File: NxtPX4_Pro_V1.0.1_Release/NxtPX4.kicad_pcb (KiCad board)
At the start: 4 copper layers, 29 x 27 mm, 165 parts, among them J1 USB_C_Receptacle_USB2.0, J10 ESC, J11 Aux GPIO, J12 AUX GPIO, J13 5V, J14 5V, J15 Aux SPI, J16 Buzz, J17 Aux I2C, J18 Aux PWM, J19 GND, J2 Receiver, J20 Aux GPIO 2, J21 GND, J22 Aux GPIO 1, J24 Micro_SD_Card, J3 5V, J4 Cam_Info, J5 9V, J6 Aux UART, J7 Aux UART, J8 Aux UART, J9 Upper computer connector, Q1 AP40P05, Q2 SS8050(NPN BEC), Q3 SS8050(NPN BEC), U1 MP9943GQ-Z, U10 BMI088, U11 ICM-20602, U12 MPU6500, U13 BMP388, U14 W25Q128JVS, U15 Signature, U16 High_temp, U17 high_voltage, U18 Caution, U19 Caution, U2 RT9013-33GB, U3 RT9013-33GB, U4 MP9943GQ-Z, U5 HKU_Logo, U6 UAV_LOGO, U7 Direction_Logo, U8 RI_LOGO, U9 STM32H743VIH6, Y1 SG-210STF/ X1G004171002700, Y2 ABS07 (32.768kHZ)

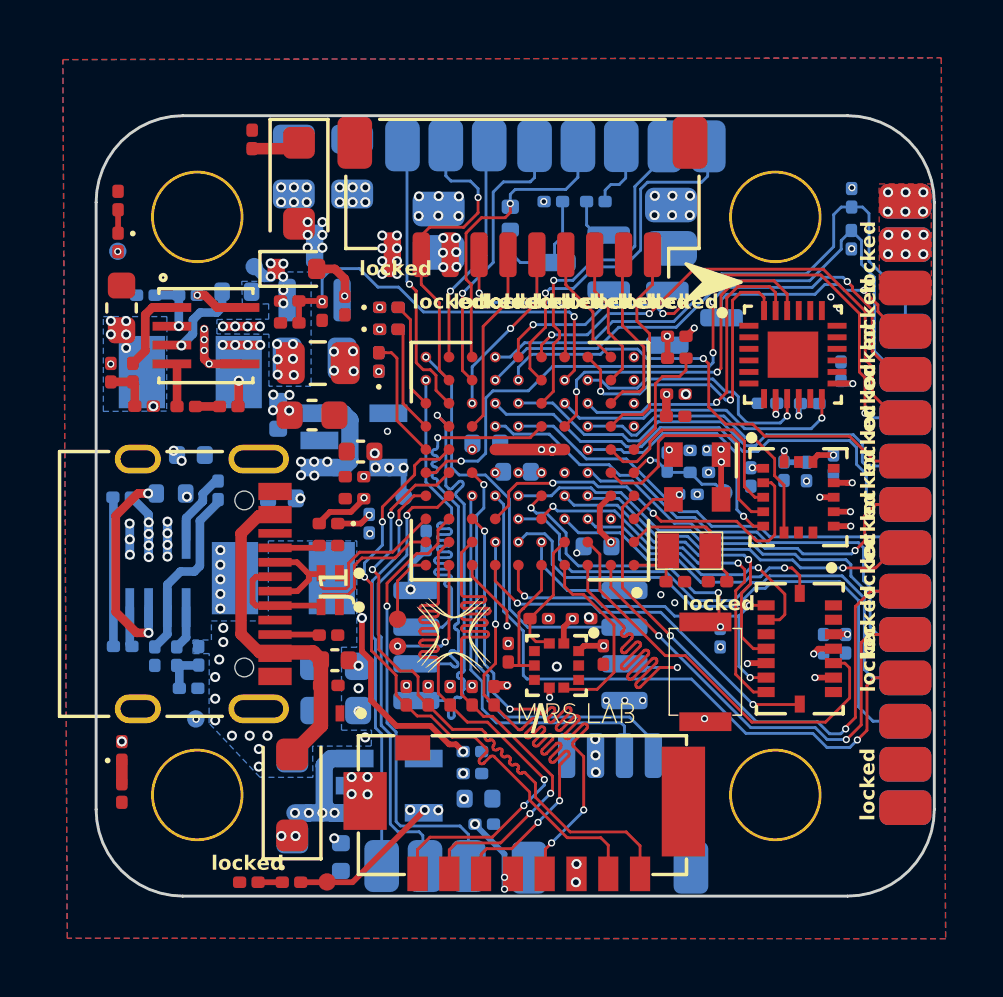
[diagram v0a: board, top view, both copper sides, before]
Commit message: [Fix][other]:Upgrade for JLC manufacturer
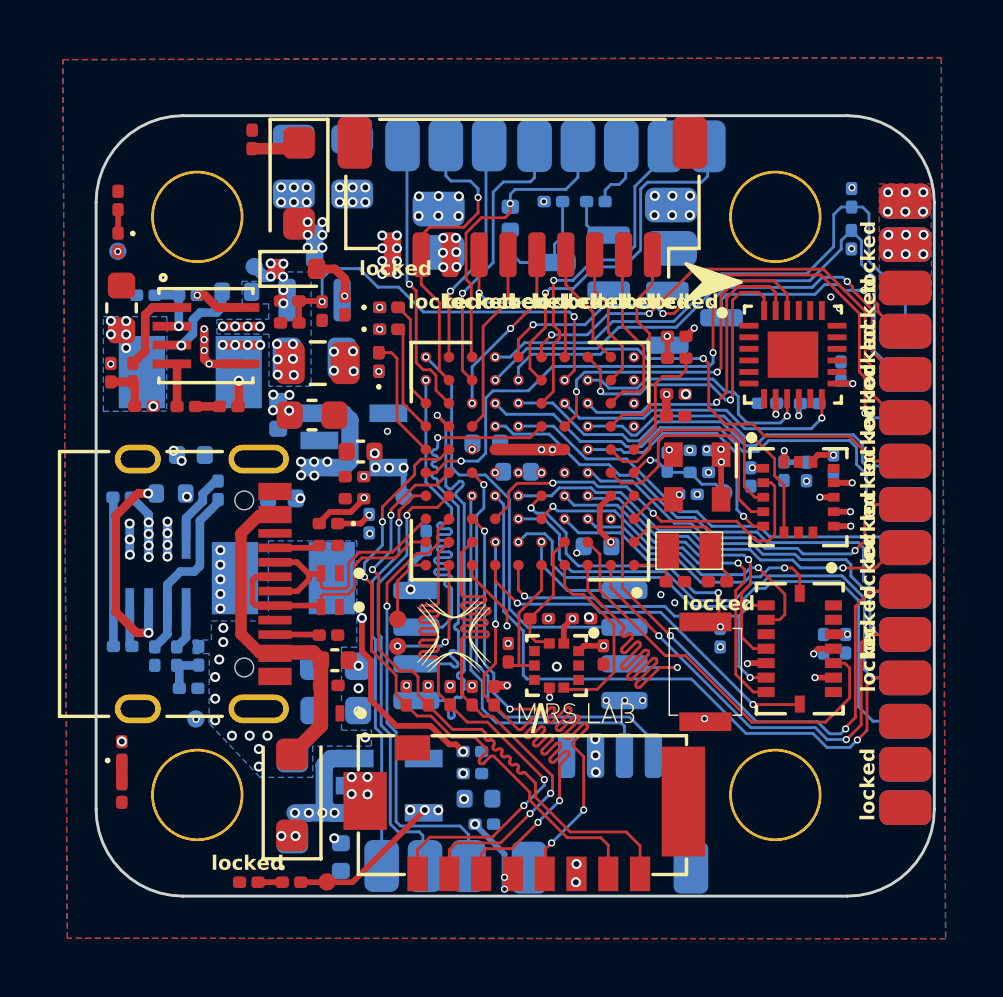
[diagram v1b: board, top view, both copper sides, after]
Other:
- board text removed: "V1.0Release"
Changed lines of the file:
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@@
   (paper "A5")
   (title_block
-    (title "NxtPX4Pro 219 V1.0")
-    (date "2023-02-19")
-    (rev "Peize")
+    (title "NxtPX4Pro 0303 V1.0.1")
+    (date "2023-03-03")
+    (rev "Khalil")
     (company "HKUST DJI")
-    (comment 1 "改善供电结构")
-    (comment 2 "增强供电能力")
-    (comment 3 "发板")
+    (comment 1 "定板")
   )
   (layers
@@
     (property "ki_keywords" "usb universal serial bus type-C USB2.0")
     (attr smd)
-    (fp_text reference "J1" (at 0 -5.715 -90) (layer "F.SilkS")
+    (fp_text reference "J1" (at 0 -5.715 -90) (layer "F.SilkS") hide
         (effects (font (size 1 1) (thickness 0.15)))
     )
@@
     )
   )
-  (footprint "NxtPX4:my_signature" (layer "B.Cu")
+  (footprint "NxtPX4:my_signature" locked (layer "B.Cu")
     (at 113.97 67.93 90)
     (property "Sheetfile" "NxtPX4.kicad_sch")
@@
     (effects (font (size 0.5 0.5) (thickness 0.1) bold) (justify left bottom mirror))
   )
-  (gr_text "V1.0Release" (at 110.25 78.78 270) (layer "B.SilkS")
+  (gr_text locked "V1.0.1\nRelease" (at 109.56 78.82 270) (layer "B.SilkS")
     (effects (font (size 0.5 0.5) (thickness 0.1) bold) (justify left bottom mirror))
   )
@@
     (effects (font (size 0.5 0.5) (thickness 0.1) bold) (justify left bottom mirror))
   )
-  (gr_text locked "GND" (at 99.9 65.11 270) (layer "B.SilkS")
+  (gr_text locked "GND" (at 99.96 65.49 270) (layer "B.SilkS")
     (effects (font (size 0.5 0.5) (thickness 0.1) bold) (justify left bottom mirror))
   )
@@
     (effects (font (size 0.5 0.5) (thickness 0.1) bold) (justify left bottom mirror))
   )
-  (gr_text locked "U5" (at 104.79 62.67 180) (layer "B.SilkS")
+  (gr_text locked "U5" (at 107.95 62.67 180) (layer "B.SilkS")
     (effects (font (size 0.5 0.5) (thickness 0.1) bold) (justify left bottom mirror))
   )
@@
     (effects (font (size 0.5 0.5) (thickness 0.1) bold) (justify left bottom mirror))
   )
-  (gr_text locked "9V" (at 99.98 63.49 270) (layer "B.SilkS")
+  (gr_text locked "9V" (at 99.96 63.67 270) (layer "B.SilkS")
     (effects (font (size 0.5 0.5) (thickness 0.1) bold) (justify left bottom mirror))
   )
@@
     (effects (font (size 0.5 0.5) (thickness 0.1) bold) (justify left bottom))
   )
-  (gr_text locked "I" (at 103.357024 66.73) (layer "F.SilkS")
+  (gr_text locked "I" (at 103.13 66.73) (layer "F.SilkS")
     (effects (font (size 0.5 0.5) (thickness 0.1) bold) (justify left bottom))
   )
-  (gr_text locked "5" (at 105.085357 66.73) (layer "F.SilkS")
+  (gr_text locked "5" (at 105.04 66.73) (layer "F.SilkS")
     (effects (font (size 0.5 0.5) (thickness 0.1) bold) (justify left bottom))
   )
@@
     (effects (font (size 0.5 0.5) (thickness 0.1) bold) (justify left bottom))
   )
-  (gr_text locked "4" (at 106.068571 66.73) (layer "F.SilkS")
+  (gr_text locked "4" (at 106.03 66.73) (layer "F.SilkS")
     (effects (font (size 0.5 0.5) (thickness 0.1) bold) (justify left bottom))
   )
@@
     (effects (font (size 0.5 0.5) (thickness 0.1) bold) (justify left bottom))
   )
-  (gr_text locked "G" (at 102.35 66.73) (layer "F.SilkS")
+  (gr_text locked "G" (at 102.02 66.73) (layer "F.SilkS")
     (effects (font (size 0.5 0.5) (thickness 0.1) bold) (justify left bottom))
   )
@@
     (effects (font (size 0.5 0.5) (thickness 0.1) bold) (justify left bottom))
   )
-  (gr_text locked "Rx" (at 100.938214 66.73) (layer "F.SilkS")
+  (gr_text locked "Rx" (at 100.79 66.73) (layer "F.SilkS")
     (effects (font (size 0.5 0.5) (thickness 0.1) bold) (justify left bottom))
   )
@@
     (effects (font (size 0.5 0.5) (thickness 0.1) bold) (justify left bottom))
   )
-  (gr_text locked "6" (at 104.102143 66.73) (layer "F.SilkS")
+  (gr_text locked "6" (at 104.01 66.73) (layer "F.SilkS")
     (effects (font (size 0.5 0.5) (thickness 0.1) bold) (justify left bottom))
   )
